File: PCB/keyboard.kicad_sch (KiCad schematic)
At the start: 152 parts, among them SW1 SW_Push, U1 ATmega32U4-A, Y1 16MHz

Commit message: fixed footprints
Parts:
- MX15, MX25, MX30, MX35, MX5, MX58: footprint MX_Alps_Hybrid:MX-1U-NoLED -> MX_Alps_Hybrid:MX-1.25U-NoLED
- MX2, MX64: footprint MX_Alps_Hybrid:MX-1U-NoLED -> MX_Alps_Hybrid:MX-1.5U-NoLED
- MX20: footprint MX_Alps_Hybrid:MX-1U-NoLED -> MX_Alps_Hybrid:MX-6.25U-NoLED
- MX3: footprint MX_Alps_Hybrid:MX-1U-NoLED -> MX_Alps_Hybrid:MX-1.75U-NoLED
- MX4, MX61: footprint MX_Alps_Hybrid:MX-1U-NoLED -> MX_Alps_Hybrid:MX-2.25U-NoLED
- MX63: footprint MX_Alps_Hybrid:MX-1U-NoLED -> MX_Alps_Hybrid:MX-2U-NoLED
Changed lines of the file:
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@@
       (effects (font (size 0.508 0.508)))
     )
-    (property "Footprint" "MX_Alps_Hybrid:MX-1U-NoLED" (id 2) (at 257.175 144.145 0)
+    (property "Footprint" "MX_Alps_Hybrid:MX-2U-NoLED" (id 2) (at 257.175 144.145 0)
       (effects (font (size 1.524 1.524)) hide)
     )
@@
       (effects (font (size 0.508 0.508)))
     )
-    (property "Footprint" "MX_Alps_Hybrid:MX-1U-NoLED" (id 2) (at 240.665 186.055 0)
+    (property "Footprint" "MX_Alps_Hybrid:MX-2.25U-NoLED" (id 2) (at 240.665 186.055 0)
       (effects (font (size 1.524 1.524)) hide)
     )
@@
       (effects (font (size 0.508 0.508)))
     )
-    (property "Footprint" "MX_Alps_Hybrid:MX-1U-NoLED" (id 2) (at 121.285 230.505 0)
+    (property "Footprint" "MX_Alps_Hybrid:MX-1.25U-NoLED" (id 2) (at 121.285 230.505 0)
       (effects (font (size 1.524 1.524)) hide)
     )
@@
       (effects (font (size 0.508 0.508)))
     )
-    (property "Footprint" "MX_Alps_Hybrid:MX-1U-NoLED" (id 2) (at 103.505 230.505 0)
+    (property "Footprint" "MX_Alps_Hybrid:MX-1.25U-NoLED" (id 2) (at 103.505 230.505 0)
       (effects (font (size 1.524 1.524)) hide)
     )
@@
       (effects (font (size 0.508 0.508)))
     )
-    (property "Footprint" "MX_Alps_Hybrid:MX-1U-NoLED" (id 2) (at 69.215 230.505 0)
+    (property "Footprint" "MX_Alps_Hybrid:MX-1.25U-NoLED" (id 2) (at 69.215 230.505 0)
       (effects (font (size 1.524 1.524)) hide)
     )
@@
       (effects (font (size 0.508 0.508)))
     )
-    (property "Footprint" "MX_Alps_Hybrid:MX-1U-NoLED" (id 2) (at 86.995 230.505 0)
+    (property "Footprint" "MX_Alps_Hybrid:MX-6.25U-NoLED" (id 2) (at 86.995 230.505 0)
       (effects (font (size 1.524 1.524)) hide)
     )
@@
       (effects (font (size 0.508 0.508)))
     )
-    (property "Footprint" "MX_Alps_Hybrid:MX-1U-NoLED" (id 2) (at 257.175 164.465 0)
+    (property "Footprint" "MX_Alps_Hybrid:MX-1.5U-NoLED" (id 2) (at 257.175 164.465 0)
       (effects (font (size 1.524 1.524)) hide)
     )
@@
       (effects (font (size 0.508 0.508)))
     )
-    (property "Footprint" "MX_Alps_Hybrid:MX-1U-NoLED" (id 2) (at 224.155 208.915 0)
+    (property "Footprint" "MX_Alps_Hybrid:MX-1.25U-NoLED" (id 2) (at 224.155 208.915 0)
       (effects (font (size 1.524 1.524)) hide)
     )
@@
       (effects (font (size 0.508 0.508)))
     )
-    (property "Footprint" "MX_Alps_Hybrid:MX-1U-NoLED" (id 2) (at 31.115 208.915 0)
+    (property "Footprint" "MX_Alps_Hybrid:MX-2.25U-NoLED" (id 2) (at 31.115 208.915 0)
       (effects (font (size 1.524 1.524)) hide)
     )
@@
       (effects (font (size 0.508 0.508)))
     )
-    (property "Footprint" "MX_Alps_Hybrid:MX-1U-NoLED" (id 2) (at 31.115 164.465 0)
+    (property "Footprint" "MX_Alps_Hybrid:MX-1.5U-NoLED" (id 2) (at 31.115 164.465 0)
       (effects (font (size 1.524 1.524)) hide)
     )
@@
       (effects (font (size 0.508 0.508)))
     )
-    (property "Footprint" "MX_Alps_Hybrid:MX-1U-NoLED" (id 2) (at 140.335 230.505 0)
+    (property "Footprint" "MX_Alps_Hybrid:MX-1.25U-NoLED" (id 2) (at 140.335 230.505 0)
       (effects (font (size 1.524 1.524)) hide)
     )
@@
       (effects (font (size 0.508 0.508)))
     )
-    (property "Footprint" "MX_Alps_Hybrid:MX-1U-NoLED" (id 2) (at 31.115 186.055 0)
+    (property "Footprint" "MX_Alps_Hybrid:MX-1.75U-NoLED" (id 2) (at 31.115 186.055 0)
       (effects (font (size 1.524 1.524)) hide)
     )
@@
       (effects (font (size 0.508 0.508)))
     )
-    (property "Footprint" "MX_Alps_Hybrid:MX-1U-NoLED" (id 2) (at 31.115 230.505 0)
+    (property "Footprint" "MX_Alps_Hybrid:MX-1.25U-NoLED" (id 2) (at 31.115 230.505 0)
       (effects (font (size 1.524 1.524)) hide)
     )
@@
     )
     (path "/b579a5a9-c6d1-48bd-84f1-5dc214d38375"
-      (reference "MX2") (unit 1) (value "MX-NoLED") (footprint "MX_Alps_Hybrid:MX-1U-NoLED")
+      (reference "MX2") (unit 1) (value "MX-NoLED") (footprint "MX_Alps_Hybrid:MX-1.5U-NoLED")
     )
     (path "/d77afc97-b763-4d8c-b6bf-0ca559a19157"
-      (reference "MX3") (unit 1) (value "MX-NoLED") (footprint "MX_Alps_Hybrid:MX-1U-NoLED")
+      (reference "MX3") (unit 1) (value "MX-NoLED") (footprint "MX_Alps_Hybrid:MX-1.75U-NoLED")
     )
     (path "/a1c7ba82-88e6-47ff-a9c4-2232fbeb6d48"
-      (reference "MX4") (unit 1) (value "MX-NoLED") (footprint "MX_Alps_Hybrid:MX-1U-NoLED")
+      (reference "MX4") (unit 1) (value "MX-NoLED") (footprint "MX_Alps_Hybrid:MX-2.25U-NoLED")
     )
     (path "/ef190a3f-72b4-49ca-a31c-14730304968e"
-      (reference "MX5") (unit 1) (value "MX-NoLED") (footprint "MX_Alps_Hybrid:MX-1U-NoLED")
+      (reference "MX5") (unit 1) (value "MX-NoLED") (footprint "MX_Alps_Hybrid:MX-1.25U-NoLED")
     )
     (path "/9489c180-9095-4e9b-9ce3-39ab9e092852"
@@
     )
     (path "/691b87b5-f243-4780-b4ff-8063b47a77e4"
-      (reference "MX15") (unit 1) (value "MX-NoLED") (footprint "MX_Alps_Hybrid:MX-1U-NoLED")
+      (reference "MX15") (unit 1) (value "MX-NoLED") (footprint "MX_Alps_Hybrid:MX-1.25U-NoLED")
     )
     (path "/420749f4-f093-427a-b007-dec9f8edd9c4"
@@
     )
     (path "/7bbd9331-b8d7-470d-8660-5ff4520c8375"
-      (reference "MX20") (unit 1) (value "MX-NoLED") (footprint "MX_Alps_Hybrid:MX-1U-NoLED")
+      (reference "MX20") (unit 1) (value "MX-NoLED") (footprint "MX_Alps_Hybrid:MX-6.25U-NoLED")
     )
     (path "/5f840a8e-d918-4cb0-9806-417e931f3ec3"
@@
     )
     (path "/5add7154-4e63-41b9-b906-ec54f8690dbb"
-      (reference "MX25") (unit 1) (value "MX-NoLED") (footprint "MX_Alps_Hybrid:MX-1U-NoLED")
+      (reference "MX25") (unit 1) (value "MX-NoLED") (footprint "MX_Alps_Hybrid:MX-1.25U-NoLED")
     )
     (path "/a06bef4c-ca33-402e-978d-b803aa6dd549"
@@
     )
     (path "/2a35ebca-9834-4e7f-b67a-d1fe902bdb26"
-      (reference "MX30") (unit 1) (value "MX-NoLED") (footprint "MX_Alps_Hybrid:MX-1U-NoLED")
+      (reference "MX30") (unit 1) (value "MX-NoLED") (footprint "MX_Alps_Hybrid:MX-1.25U-NoLED")
     )
     (path "/0fd9f6ac-5f71-43bd-8ab8-8b28121df25c"
@@
     )
     (path "/ce5c33f0-fd55-4141-beea-fc38e03c4a12"
-      (reference "MX35") (unit 1) (value "MX-NoLED") (footprint "MX_Alps_Hybrid:MX-1U-NoLED")
+      (reference "MX35") (unit 1) (value "MX-NoLED") (footprint "MX_Alps_Hybrid:MX-1.25U-NoLED")
     )
     (path "/97e3d1f8-85a4-40ab-a7c4-773394d227e3"
@@
     )
     (path "/81b6bdbf-481a-4613-94c1-dce831f0fcfe"
-      (reference "MX58") (unit 1) (value "MX-NoLED") (footprint "MX_Alps_Hybrid:MX-1U-NoLED")
+      (reference "MX58") (unit 1) (value "MX-NoLED") (footprint "MX_Alps_Hybrid:MX-1.25U-NoLED")
     )
     (path "/f1de1179-e025-4787-9175-a16c216071eb"
@@
     )
     (path "/165d459a-a80c-46e6-946c-add18f788982"
-      (reference "MX61") (unit 1) (value "MX-NoLED") (footprint "MX_Alps_Hybrid:MX-1U-NoLED")
+      (reference "MX61") (unit 1) (value "MX-NoLED") (footprint "MX_Alps_Hybrid:MX-2.25U-NoLED")
     )
     (path "/8b5c8579-bebf-4069-82e9-fb68f50a3f97"
@@
     )
     (path "/062e085b-8f23-45fa-ada8-23a80f61f29b"
-      (reference "MX63") (unit 1) (value "MX-NoLED") (footprint "MX_Alps_Hybrid:MX-1U-NoLED")
+      (reference "MX63") (unit 1) (value "MX-NoLED") (footprint "MX_Alps_Hybrid:MX-2U-NoLED")
     )
     (path "/80b547f7-6e38-477e-a098-e02075564787"
-      (reference "MX64") (unit 1) (value "MX-NoLED") (footprint "MX_Alps_Hybrid:MX-1U-NoLED")
+      (reference "MX64") (unit 1) (value "MX-NoLED") (footprint "MX_Alps_Hybrid:MX-1.5U-NoLED")
     )
     (path "/e7c00da9-1fab-49a9-a0ef-e747f94b741d"

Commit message: PCB work in progress
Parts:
- MX58: footprint MX_Alps_Hybrid:MX-1.25U-NoLED -> MX_Alps_Hybrid:MX-2.25U-NoLED
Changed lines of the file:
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@@
       (effects (font (size 0.508 0.508)))
     )
-    (property "Footprint" "MX_Alps_Hybrid:MX-1.25U-NoLED" (id 2) (at 224.155 208.915 0)
+    (property "Footprint" "MX_Alps_Hybrid:MX-2.25U-NoLED" (id 2) (at 224.155 208.915 0)
       (effects (font (size 1.524 1.524)) hide)
     )
@@
     )
     (path "/81b6bdbf-481a-4613-94c1-dce831f0fcfe"
-      (reference "MX58") (unit 1) (value "MX-NoLED") (footprint "MX_Alps_Hybrid:MX-1.25U-NoLED")
+      (reference "MX58") (unit 1) (value "MX-NoLED") (footprint "MX_Alps_Hybrid:MX-2.25U-NoLED")
     )
     (path "/f1de1179-e025-4787-9175-a16c216071eb"

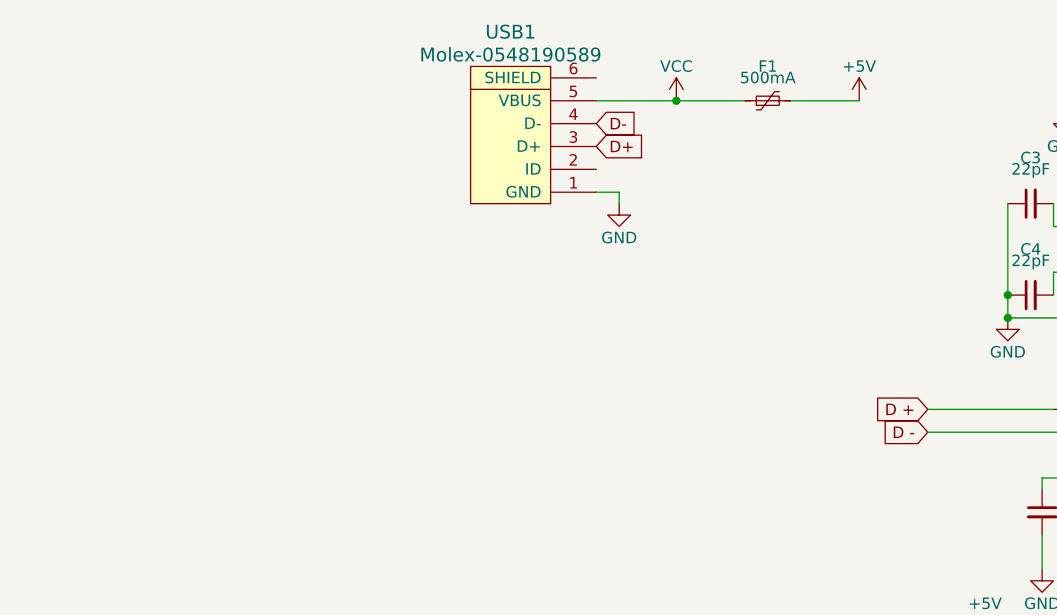
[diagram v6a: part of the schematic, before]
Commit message: updated schematic to work with unified daughterboard
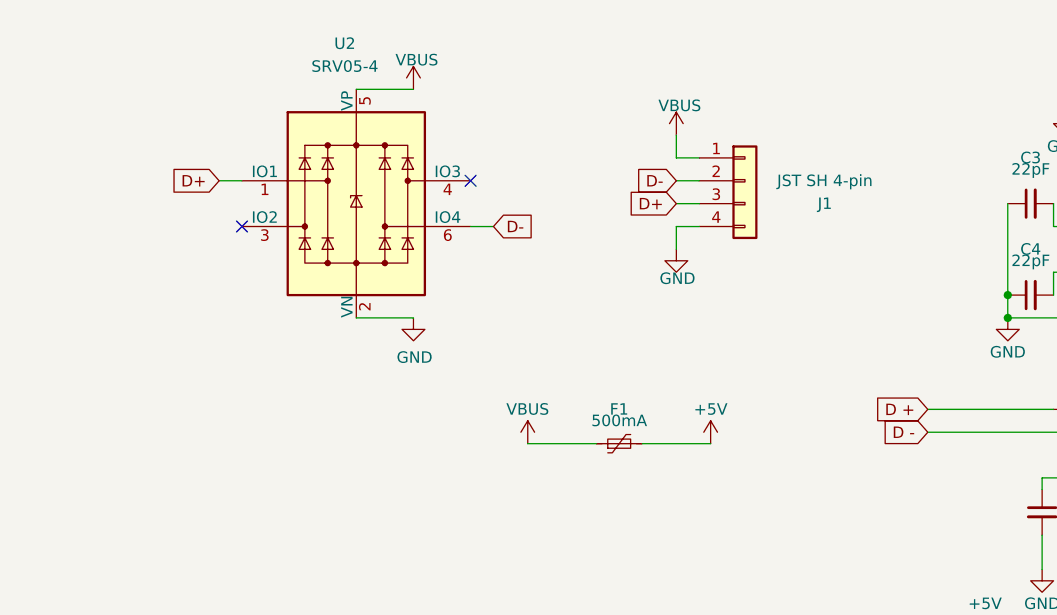
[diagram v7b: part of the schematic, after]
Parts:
- removed USB1: Molex-0548190589, random-keyboard-parts:Molex-0548190589, symbol random-keyboard-parts:Molex-0548190589
- added J1: JST SH 4-pin, Connector_JST:JST_SH_SM04B-SRSS-TB_1x04-1MP_P1.00mm_Horizontal, symbol Connector_Generic:Conn_01x04
- added U2: SRV05-4, Package_TO_SOT_SMD:SOT-23-6, symbol Power_Protection:SRV05-4
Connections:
- net D+: now also J1.3 (Pin_3), U2.1 (IO1)
- net D-: now also J1.2 (Pin_2), U2.6 (IO4)
- net GND: now also J1.4 (Pin_4), U2.2 (VN)
- net VCC renamed VBUS
- net VBUS: now also J1.1 (Pin_1), U2.5 (VP)
- no-connect marks 0 -> 2
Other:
- moved on the sheet: F1

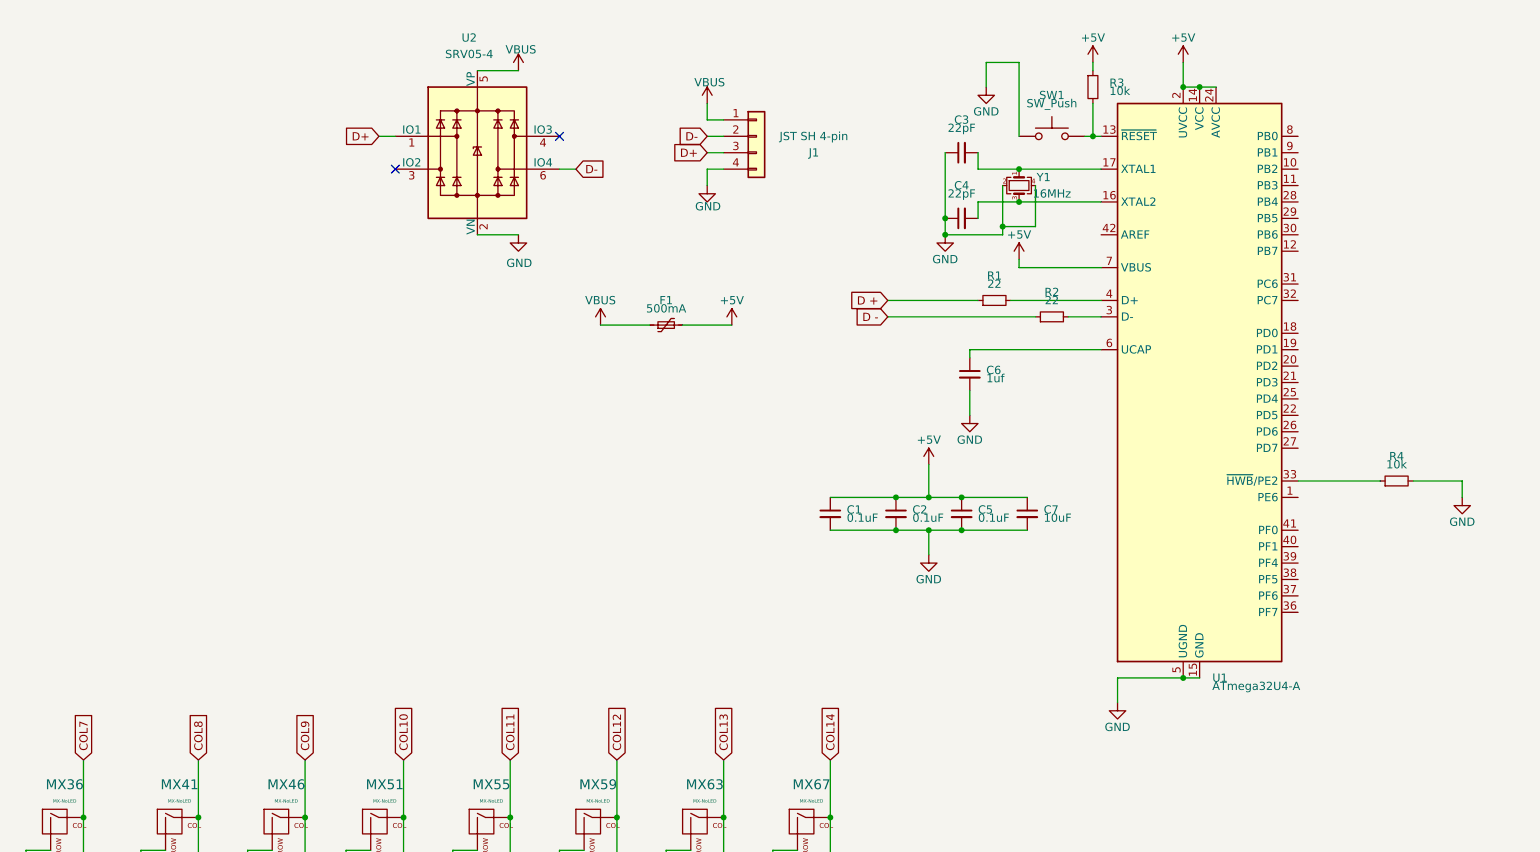
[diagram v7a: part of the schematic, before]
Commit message: changed pcb to work with unified daughterboard
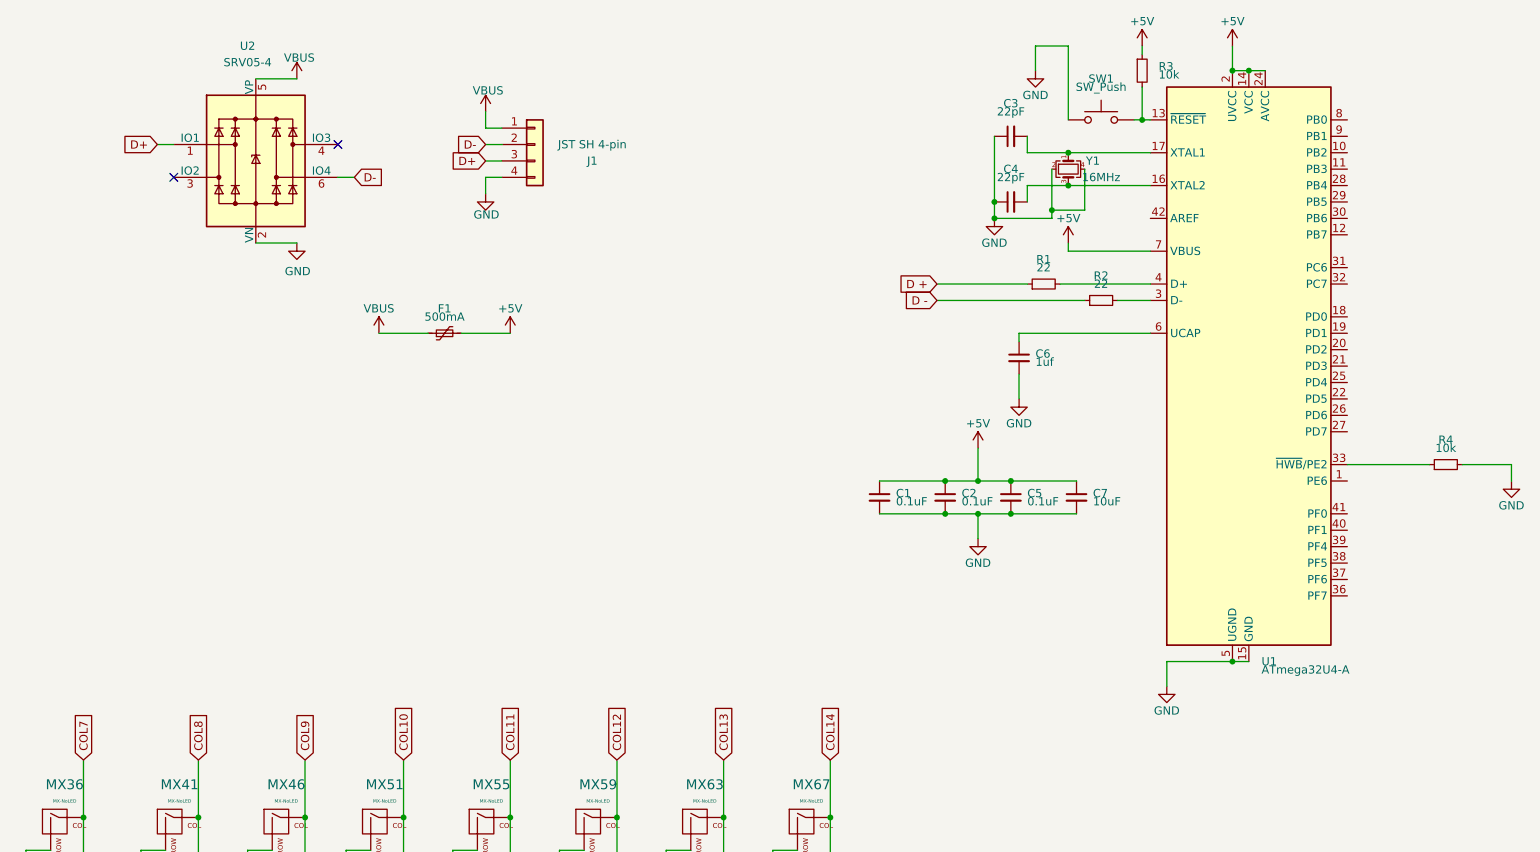
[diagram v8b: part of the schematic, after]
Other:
- moved on the sheet: C1, C2, C3, C4, C5, C6, C7, F1, J1, R1, R2, R3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
